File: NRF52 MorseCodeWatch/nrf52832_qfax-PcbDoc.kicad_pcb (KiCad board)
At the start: 2 copper layers, 17.8 x 13.7 mm, 23 parts, among them J1 Conn_01x04, U1 NRF52832-QFAA-R, U2 AT42QT1010-TSHR, X1 32mHz, X2 32.768kHz

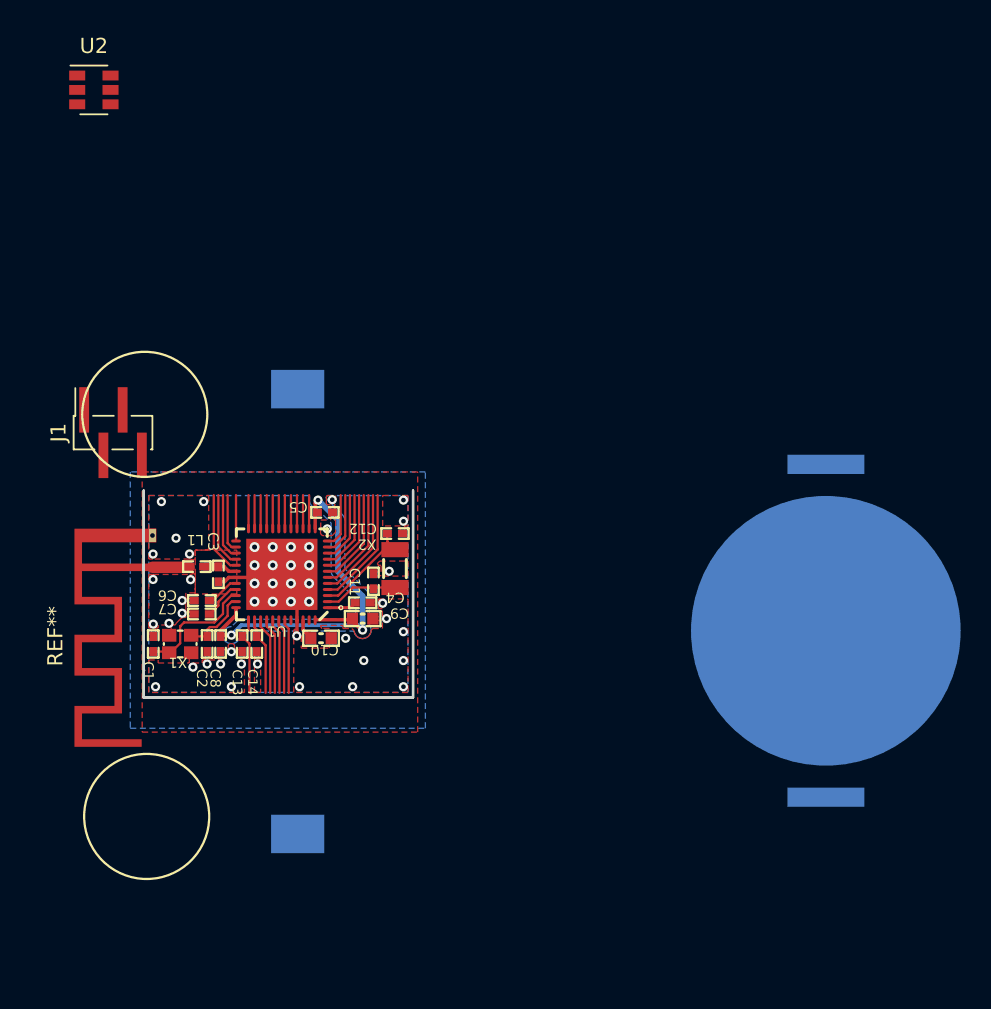
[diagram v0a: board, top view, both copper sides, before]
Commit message: adding correct ground
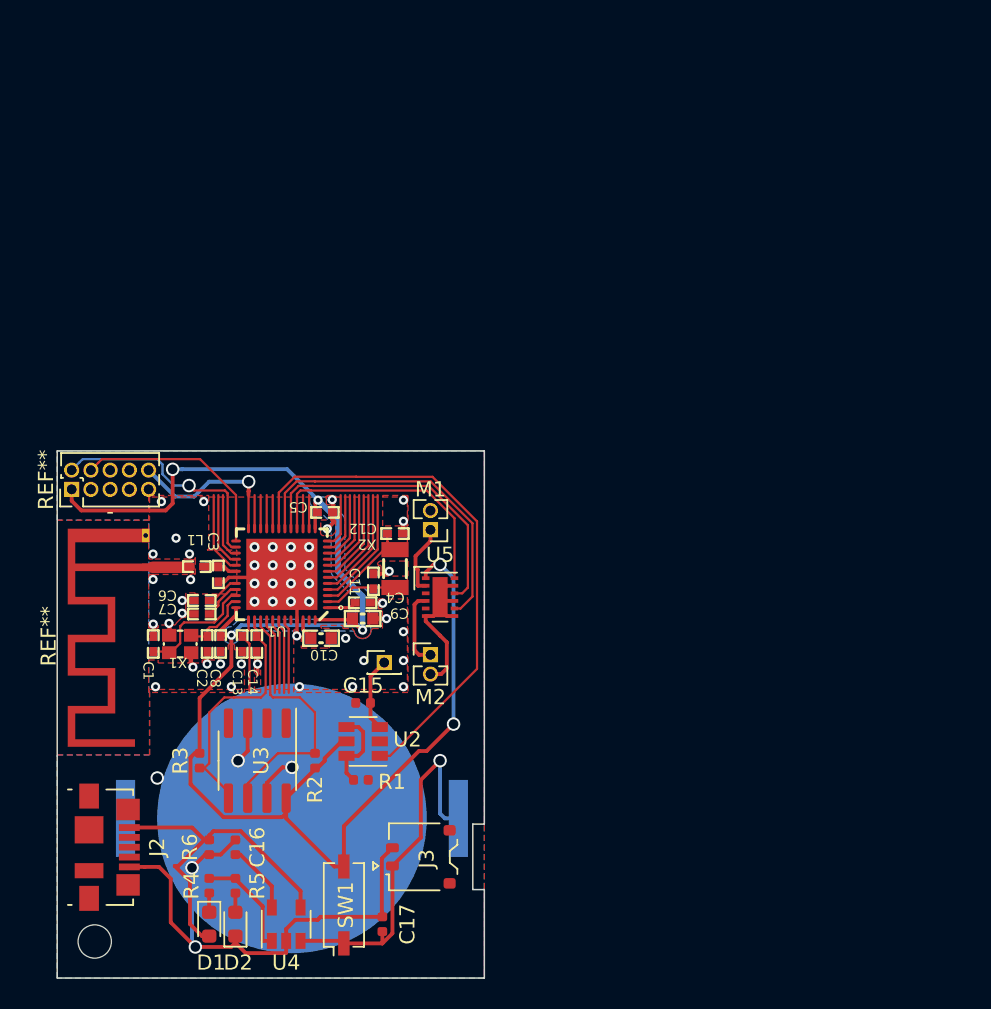
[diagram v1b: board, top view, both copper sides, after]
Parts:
- removed J1: Conn_01x04, Connector_PinHeader_1.27mm:PinHeader_1x04_P1.27mm_Vertical_SMD_Pin1Right
- removed the REF** at (100.5, 73.3)
- added C15: 22pF, Capacitor_SMD:C_0402_1005Metric, F.Cu at (104.8, 79.4)
- added C16: C 10uf, Capacitor_SMD:C_0402_1005Metric, F.Cu at (94.6, 88.9)
- added C17: C 10uf, Capacitor_SMD:C_0402_1005Metric, F.Cu at (106.0, 94.0)
- added D1: LED RED, LED_SMD:LED_0603_1608Metric, F.Cu at (94.6, 94.0)
- added D2: LED GREEN, LED_SMD:LED_0603_1608Metric, F.Cu at (96.3, 94.0)
- added J2: USB_B_Micro, Connector_USB:USB_Micro-B_Molex_47346-0001, F.Cu at (87.9, 88.9)
- added J3: Conn_01x02_Male LiPo Battery, Connector_JST:JST_ACH_BM02B-ACHSS-GAN-ETF_1x02-1MP_P1.20mm_Vertical, F.Cu at (108.6, 89.5)
- added M1: Motor_DC, Connector_PinHeader_1.27mm:PinHeader_1x02_P1.27mm_Vertical, F.Cu at (109.2, 67.9)
- added M2: Motor_DC, Connector_PinHeader_1.27mm:PinHeader_1x02_P1.27mm_Vertical, F.Cu at (109.2, 76.2)
- added R1: 1K, Resistor_SMD:R_0402_1005Metric, F.Cu at (104.6, 84.5)
- added R2: 10K, Resistor_SMD:R_0402_1005Metric, F.Cu at (101.6, 83.2)
- added R3: 10K, Resistor_SMD:R_0402_1005Metric, F.Cu at (94.0, 83.2)
- added R4: R, Resistor_SMD:R_0402_1005Metric, F.Cu at (94.6, 91.4)
- added R5: R, Resistor_SMD:R_0402_1005Metric, F.Cu at (96.3, 91.4)
- added R6: R 10K, Resistor_SMD:R_0402_1005Metric, F.Cu at (96.3, 88.9)
- added REF**: PinHeader_2x05_P1.27mm_Vertical, Connector_PinHeader_1.27mm:PinHeader_2x05_P1.27mm_Vertical, F.Cu at (85.5, 65.3)
- added REF**: PinHeader_1x01_P1.27mm_Vertical, Connector_PinHeader_1.27mm:PinHeader_1x01_P1.27mm_Vertical, F.Cu at (106.2, 76.7)
- added REF**: MountingHole_2.2mm_M2, MountingHole:MountingHole_2.2mm_M2, F.Cu at (87.1, 95.1)
- added SW1: SW_DIP_x01, Button_Switch_SMD:SW_DIP_SPSTx01_Slide_Copal_CHS-01A_W5.08mm_P1.27mm_JPin, F.Cu at (103.5, 92.7)
- added U3: CAT24C256, Package_SO:SOIC-8_3.9x4.9mm_P1.27mm, F.Cu at (97.8, 83.2)
- added U4: MCP73831-2-OT, Package_TO_SOT_SMD:SOT-23-5, F.Cu at (99.7, 94.0)
- added U5: DRV8836, Package_SON:WSON-12-1EP_3x2mm_P0.5mm_EP1x2.65, F.Cu at (109.9, 72.4)
- moved U2 46.5 mm to (104.8, 81.9), turned to 180 degrees
- moved J5 37.4 mm to (100.1, 87.0), turned to 0 degrees
- moved REF** 0.44 mm to (90.4, 70.4)
- renumbered REF** to J5
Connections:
- J5 pad 1: (no net) -> /VBAT-IN
- J5 pad 2: (no net) -> GND
- U1 pad 16: /P0.13 -> /Motor_Sleep
- U1 pad 17: /P0.14 -> /Motor1
- U1 pad 18: /P0.15 -> /Motor2
- U1 pad 19: /P0.16 -> /MainSwitch
- X1 pad 3: (no net) -> GND
- X1 pad 4: (no net) -> GND
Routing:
- net /VDD_nRF: track 27.3 -> 105.0 mm, vias 3 -> 6
- net GND: track 5.56 -> 81.8 mm, vias 17 -> 54
- net /MainSwitch: track 0.00 -> 35.6 mm
- net /VBAT-IN: track 0.00 -> 24.7 mm, vias 0 -> 1
- net /VCC: track 0.00 -> 23.3 mm
- net /Motor2: track 0.00 -> 22.5 mm
- net /Motor1: track 0.00 -> 20.4 mm
- net /Motor_Sleep: track 0.00 -> 17.5 mm
- net /P0.27: track 5.06 -> 17.6 mm
- net /SWDIO: track 3.83 -> 15.9 mm, vias 0 -> 1
- net /P0.26: track 5.13 -> 16.1 mm
- net /SWDCLK: track 3.03 -> 13.9 mm
- net /P0.21: track 2.21 -> 10.8 mm, vias 0 -> 1
- net /STAT: track 0.00 -> 7.25 mm
- net /TOG-AHLB: track 0.00 -> 5.51 mm
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- added copper zone on B.Cu, net GND
- added copper zone on F.Cu, net GND
- removed copper zone on B.Cu, net (none)
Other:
- board size 17.8 x 13.7 mm -> 28.2 x 34.8 mm
- net class slim added: clearance 0.1524, trace_width 0.15, via_dia 0.889, via_drill 0.635
- rule trace_min: 0.254 -> 0.15
- board text added: "-"

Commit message: minor fixes
minor layout changes to pcb
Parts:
- added C18: C 10uf, Capacitor_SMD:C_0402_1005Metric, F.Cu at (111.3, 75.5)
- moved M2 1.40 mm to (109.3, 77.6), turned to 180 degrees
- turned J5 to 180 degrees
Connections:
- M1 pad 2: GND -> /Motor1_outB
- M2 pad 2: GND -> /Motor2_outB
- U1 pad 15: /P0.12 -> /Motor_Sleep
- U1 pad 16: /Motor_Sleep -> /Motor_Mode
- U1 pad 17: /Motor1 -> /Motor1_ENBL
- U1 pad 18: /Motor2 -> /Motor2_ENBL
- U5 pad 10: /Motor1 -> /Motor1_PHASE
- U5 pad 11: GND -> /Motor_Mode
- U5 pad 7: GND -> /Motor2_ENBL
- U5 pad 8: /Motor2 -> /Motor2_PHASE
- U5 pad 9: GND -> /Motor1_ENBL
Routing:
- net /Motor2_ENBL: track 0.00 -> 23.9 mm
- net /Motor2: track 22.5 -> 0.00 mm
- net /Motor1_ENBL: track 0.00 -> 21.8 mm
- net /Motor1: track 20.4 -> 0.00 mm
- net /Motor_Mode: track 0.00 -> 19.6 mm
- net GND: track 81.8 -> 72.1 mm
- net /Motor1_outB: track 0.00 -> 6.89 mm
- net /Motor2_outB: track 0.00 -> 4.00 mm
- net /VDD_nRF: track 105.0 -> 108.2 mm, vias 6 -> 7
- net /P0.12: track 2.21 -> 0.00 mm
- net /Motor2_out: track 5.04 -> 6.40 mm
- net /MainSwitch: track 35.6 -> 36.9 mm
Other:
- outline, holes or cut-outs redrawn

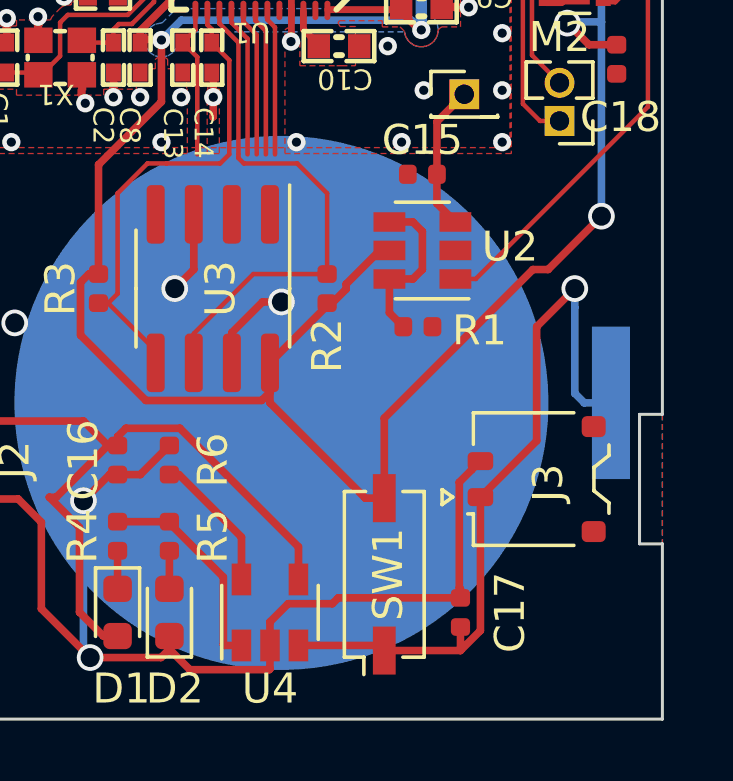
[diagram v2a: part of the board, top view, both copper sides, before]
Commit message: adding routing for a jst connection
adding routing for a jst connection to the touchpad, and a test prob area for the battery
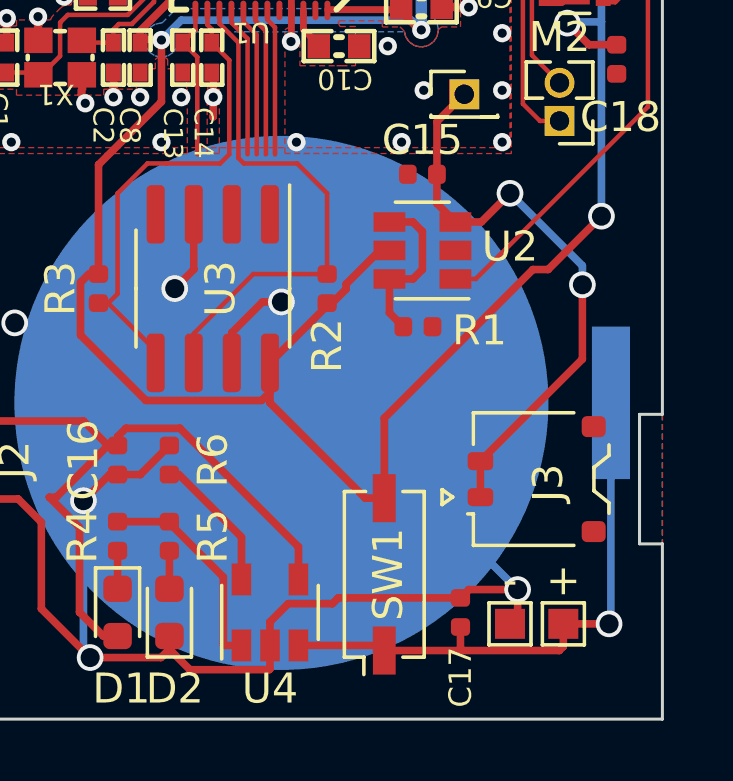
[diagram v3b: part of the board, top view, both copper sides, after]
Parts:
- added +: TestPoint_Pad_1.0x1.0mm, TestPoint:TestPoint_Pad_1.0x1.0mm, F.Cu at (109.5, 94.4)
- added -: TestPoint_Pad_1.0x1.0mm, TestPoint:TestPoint_Pad_1.0x1.0mm, F.Cu at (107.7, 94.4)
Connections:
- J3 pad 1: /VBAT-IN -> /TouchPad
- J3 pad 2: GND -> /TouchPad
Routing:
- net /TouchPad: track 4.89 -> 19.6 mm, vias 0 -> 2
- net GND: track 72.1 -> 80.9 mm, vias 54 -> 55
- net /VBAT-IN: track 24.7 -> 19.6 mm
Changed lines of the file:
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@@
     (thickness 1.6)
     (drawings 314)
-    (tracks 467)
+    (tracks 476)
     (zones 0)
-    (modules 44)
+    (modules 46)
     (nets 65)
   )
@@
     (mod_text_size 1 1)
     (mod_text_width 0.15)
-    (pad_size 0.59 0.64)
+    (pad_size 0.6 0.85)
     (pad_drill 0)
     (pad_to_mask_clearance 0)
@@
     (add_net /SWDIO)
   )
+  (module TestPoint:TestPoint_Pad_1.0x1.0mm (layer F.Cu)
+    (at 107.696 94.361)
+    (descr "SMD rectangular pad as test Point, square 1.0mm side length")
+    (tags "test point SMD pad rectangle square")
+    (attr virtual)
+    (fp_text reference - (at 0 -1.448) (layer F.SilkS)
+      (effects (font (size 1 1) (thickness 0.15)))
+    )
+    (fp_text value TestPoint_Pad_1.0x1.0mm (at 0 1.55) (layer F.Fab)
+      (effects (font (size 1 1) (thickness 0.15)))
+    )
+    (fp_line (start 1 1) (end -1 1) (layer F.CrtYd) (width 0.05))
+    (fp_line (start 1 1) (end 1 -1) (layer F.CrtYd) (width 0.05))
+    (fp_line (start -1 -1) (end -1 1) (layer F.CrtYd) (width 0.05))
+    (fp_line (start -1 -1) (end 1 -1) (layer F.CrtYd) (width 0.05))
+    (fp_line (start -0.7 0.7) (end -0.7 -0.7) (layer F.SilkS) (width 0.12))
+    (fp_line (start 0.7 0.7) (end -0.7 0.7) (layer F.SilkS) (width 0.12))
+    (fp_line (start 0.7 -0.7) (end 0.7 0.7) (layer F.SilkS) (width 0.12))
+    (fp_line (start -0.7 -0.7) (end 0.7 -0.7) (layer F.SilkS) (width 0.12))
+    (fp_text user %R (at 0 -1.45) (layer F.Fab)
+      (effects (font (size 1 1) (thickness 0.15)))
+    )
+    (pad 1 smd rect (at 0 0) (size 1 1) (layers F.Cu F.Mask)
+      (net 3 GND))
+  )
+  (module TestPoint:TestPoint_Pad_1.0x1.0mm (layer F.Cu)
+    (at 109.474 94.361)
+    (descr "SMD rectangular pad as test Point, square 1.0mm side length")
+    (tags "test point SMD pad rectangle square")
+    (attr virtual)
+    (fp_text reference + (at 0 -1.448) (layer F.SilkS)
+      (effects (font (size 1 1) (thickness 0.15)))
+    )
+    (fp_text value TestPoint_Pad_1.0x1.0mm (at 0 1.55) (layer F.Fab)
+      (effects (font (size 1 1) (thickness 0.15)))
+    )
+    (fp_line (start 1 1) (end -1 1) (layer F.CrtYd) (width 0.05))
+    (fp_line (start 1 1) (end 1 -1) (layer F.CrtYd) (width 0.05))
+    (fp_line (start -1 -1) (end -1 1) (layer F.CrtYd) (width 0.05))
+    (fp_line (start -1 -1) (end 1 -1) (layer F.CrtYd) (width 0.05))
+    (fp_line (start -0.7 0.7) (end -0.7 -0.7) (layer F.SilkS) (width 0.12))
+    (fp_line (start 0.7 0.7) (end -0.7 0.7) (layer F.SilkS) (width 0.12))
+    (fp_line (start 0.7 -0.7) (end 0.7 0.7) (layer F.SilkS) (width 0.12))
+    (fp_line (start -0.7 -0.7) (end 0.7 -0.7) (layer F.SilkS) (width 0.12))
+    (fp_text user %R (at 0 -1.45) (layer F.Fab)
+      (effects (font (size 1 1) (thickness 0.15)))
+    )
+    (pad 1 smd rect (at 0 0) (size 1 1) (layers F.Cu F.Mask)
+      (net 40 /VBAT-IN))
+  )
   (module QFN40P600X600X90-48N (layer F.Cu)
     (at 99.40906 70.88662 180)
@@
     (tags capacitor)
     (attr smd)
-    (fp_text reference C17 (at 0 1.651 90) (layer F.SilkS)
-      (effects (font (size 1 1) (thickness 0.15)))
+    (fp_text reference C17 (at -2.159 0 90) (layer F.SilkS)
+      (effects (font (size 0.75 0.75) (thickness 0.1)))
     )
     (fp_text value "C 10uf" (at 0 1.17 90) (layer F.Fab)
@@
     )
     (pad 1 smd roundrect (at -0.6 -1.875 90) (size 0.6 0.85) (layers F.Cu F.Paste F.Mask) (roundrect_rratio 0.25)
-      (net 40 /VBAT-IN))
+      (net 37 /TouchPad))
     (pad 2 smd roundrect (at 0.6 -1.875 90) (size 0.6 0.85) (layers F.Cu F.Paste F.Mask) (roundrect_rratio 0.25)
-      (net 3 GND))
+      (net 37 /TouchPad))
     (pad MP smd roundrect (at -1.75 1.9 90) (size 0.7 0.8) (layers F.Cu F.Paste F.Mask) (roundrect_rratio 0.25))
     (pad MP smd roundrect (at 1.75 1.9 90) (size 0.7 0.8) (layers F.Cu F.Paste F.Mask) (roundrect_rratio 0.25))
@@
   (segment (start 92.075 90.971) (end 91.304 90.2) (width 0.254) (layer F.Cu) (net 3))
   (segment (start 92.075 93.859) (end 92.075 90.971) (width 0.254) (layer F.Cu) (net 3))
-  (segment (start 106.411959 89.233041) (end 106.71 88.935) (width 0.254) (layer F.Cu) (net 3))
-  (segment (start 106.00559 89.63941) (end 106.411959 89.233041) (width 0.254) (layer F.Cu) (net 3))
-  (segment (start 106.00559 93.16059) (end 106.00559 89.63941) (width 0.254) (layer F.Cu) (net 3))
-  (segment (start 106.045 93.2) (end 106.00559 93.16059) (width 0.254) (layer F.Cu) (net 3))
-  (segment (start 106.045 93.495) (end 106.045 93.2) (width 0.254) (layer F.Cu) (net 3))
   (segment (start 90.36 90.2) (end 89.344 90.2) (width 0.254) (layer F.Cu) (net 3))
   (segment (start 91.97462 74.13221) (end 91.96302 74.12061) (width 0.254) (layer F.Cu) (net 3))
@@
   (segment (start 109.409 73.64) (end 108.905 73.64) (width 0.254) (layer F.Cu) (net 3))
   (segment (start 109.855 73.194) (end 109.409 73.64) (width 0.254) (layer F.Cu) (net 3))
+  (via (at 107.95 93.218) (size 0.889) (drill 0.635) (layers F.Cu B.Cu) (net 3))
+  (segment (start 100.076 86.995) (end 101.727 86.995) (width 0.254) (layer B.Cu) (net 3))
+  (segment (start 101.727 86.995) (end 107.95 93.218) (width 0.254) (layer B.Cu) (net 3))
+  (segment (start 106.322 93.218) (end 106.045 93.495) (width 0.254) (layer F.Cu) (net 3))
+  (segment (start 107.95 93.218) (end 106.322 93.218) (width 0.254) (layer F.Cu) (net 3))
+  (segment (start 107.95 94.107) (end 107.696 94.361) (width 0.254) (layer F.Cu) (net 3))
+  (segment (start 107.95 93.218) (end 107.95 94.107) (width 0.254) (layer F.Cu) (net 3))
   (segment (start 95.09122 74.36661) (end 94.65528 74.36661) (width 0.1524) (layer F.Cu) (net 4))
   (segment (start 95.83046 73.62736) (end 95.09122 74.36661) (width 0.1524) (layer F.Cu) (net 4))
@@
   (segment (start 105.26 77.62) (end 106.172 76.708) (width 0.254) (layer F.Cu) (net 37))
   (segment (start 105.26 79.375) (end 105.26 77.62) (width 0.254) (layer F.Cu) (net 37))
+  (segment (start 105.875 80.965) (end 106.741 80.965) (width 0.254) (layer F.Cu) (net 37))
+  (via (at 107.696 80.01) (size 0.889) (drill 0.635) (layers F.Cu B.Cu) (net 37))
+  (segment (start 106.741 80.965) (end 107.696 80.01) (width 0.254) (layer F.Cu) (net 37))
+  (segment (start 107.696 80.01) (end 110.109 82.423) (width 0.254) (layer B.Cu) (net 37))
+  (via (at 110.109 83.058) (size 0.889) (drill 0.635) (layers F.Cu B.Cu) (net 37))
+  (segment (start 110.109 82.423) (end 110.109 83.058) (width 0.254) (layer B.Cu) (net 37))
+  (segment (start 110.109 85.536) (end 106.71 88.935) (width 0.254) (layer F.Cu) (net 37))
+  (segment (start 110.109 83.058) (end 110.109 85.536) (width 0.254) (layer F.Cu) (net 37))
+  (segment (start 106.71 90.135) (end 106.71 88.935) (width 0.254) (layer F.Cu) (net 37))
   (segment (start 104.459 80.965) (end 104.775 81.281) (width 0.254) (layer F.Cu) (net 38))
   (segment (start 103.675 80.965) (end 104.459 80.965) (width 0.254) (layer F.Cu) (net 38))
@@
   (segment (start 96.3422 90.955) (end 96.295942 90.955) (width 0.254) (layer F.Cu) (net 39))
   (segment (start 96.3422 90.955) (end 94.615 90.955) (width 0.254) (layer F.Cu) (net 39))
-  (via (at 109.855 83.185) (size 0.889) (drill 0.635) (layers F.Cu B.Cu) (net 40))
-  (segment (start 109.855 83.185) (end 108.585 84.455) (width 0.254) (layer F.Cu) (net 40))
   (segment (start 106.045 94.465) (end 106.045 95.25) (width 0.254) (layer F.Cu) (net 40))
   (segment (start 103.505 95.25) (end 106.045 95.25) (width 0.254) (layer F.Cu) (net 40))
-  (segment (start 106.71 94.585) (end 106.71 90.135) (width 0.254) (layer F.Cu) (net 40))
-  (segment (start 106.045 95.25) (end 106.71 94.585) (width 0.254) (layer F.Cu) (net 40))
-  (segment (start 108.585 88.26) (end 106.71 90.135) (width 0.254) (layer F.Cu) (net 40))
-  (segment (start 108.585 84.455) (end 108.585 88.26) (width 0.254) (layer F.Cu) (net 40))
-  (segment (start 109.855 83.813617) (end 109.855 83.185) (width 0.254) (layer B.Cu) (net 40))
-  (segment (start 109.855 86.678) (end 109.855 83.813617) (width 0.254) (layer B.Cu) (net 40))
-  (segment (start 110.172 86.995) (end 109.855 86.678) (width 0.254) (layer B.Cu) (net 40))
-  (segment (start 111.061 86.995) (end 110.172 86.995) (width 0.254) (layer B.Cu) (net 40))
   (segment (start 103.335 95.08) (end 103.505 95.25) (width 0.254) (layer F.Cu) (net 40))
   (segment (start 100.645 95.08) (end 103.335 95.08) (width 0.254) (layer F.Cu) (net 40))
+  (via (at 110.998 94.361) (size 0.889) (drill 0.635) (layers F.Cu B.Cu) (net 40))
+  (segment (start 111.061 86.995) (end 111.061 94.298) (width 0.254) (layer B.Cu) (net 40))
+  (segment (start 111.061 94.298) (end 110.998 94.361) (width 0.254) (layer B.Cu) (net 40))
+  (segment (start 106.149 94.361) (end 106.045 94.465) (width 0.254) (layer F.Cu) (net 40))
+  (segment (start 110.998 94.361) (end 109.474 94.361) (width 0.254) (layer F.Cu) (net 40))
+  (segment (start 109.474 95.115) (end 109.474 94.361) (width 0.254) (layer F.Cu) (net 40))
+  (segment (start 109.339 95.25) (end 109.474 95.115) (width 0.254) (layer F.Cu) (net 40))
+  (segment (start 106.045 95.25) (end 109.339 95.25) (width 0.254) (layer F.Cu) (net 40))
   (segment (start 94.14 94.7675) (end 93.345 93.9725) (width 0.254) (layer F.Cu) (net 41))
   (segment (start 94.615 94.7675) (end 94.14 94.7675) (width 0.254) (layer F.Cu) (net 41))
